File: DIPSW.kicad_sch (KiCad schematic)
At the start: 4 parts, among them SW1 OSCSEL

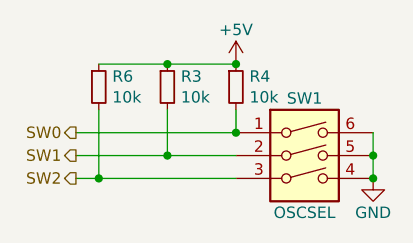
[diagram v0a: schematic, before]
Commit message: Migrate to KiCAD 6
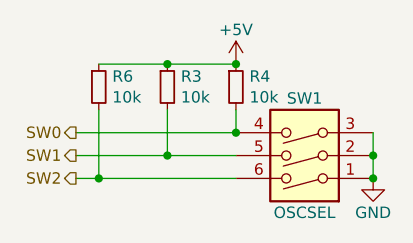
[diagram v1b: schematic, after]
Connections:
- net GND: now also SW1.1, SW1.2, SW1.3; no longer SW1.4, SW1.5, SW1.6
- net SW0: now also SW1.4; no longer SW1.1
- net SW1: now also SW1.5; no longer SW1.2
- net SW2: now also SW1.6; no longer SW1.3
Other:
- moved on the sheet: SW1
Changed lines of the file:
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@@
     (effects (font (size 1.27 1.27)) (justify right))
   )
-  (symbol (lib_id "Switch:SW_DIP_x03") (at 110.49 91.44 0)
+  (symbol (lib_id "Switch:SW_DIP_x03") (at 110.49 86.36 180) (unit 1)
     (in_bom yes) (on_board yes)
     (property "Reference" "SW1" (id 0) (at 110.49 82.55 0))
     (property "Value" "OSCSEL" (id 1) (at 110.49 95.25 0))
-    (property "Footprint" "stdpads:SW_DIP_SPSTx03_Slide_DSHP03TS_P1.27mm" (id 2) (at 110.49 91.44 0)
+    (property "Footprint" "stdpads:SW_DIP_SPSTx03_Slide_DSHP03TS_P1.27mm" (id 2) (at 110.49 86.36 0)
       (effects (font (size 1.27 1.27)) hide)
     )
-    (property "Datasheet" "~" (id 3) (at 110.49 91.44 0)
+    (property "Datasheet" "~" (id 3) (at 110.49 86.36 0)
       (effects (font (size 1.27 1.27)) hide)
     )
-    (property "LCSC Part" "C319051" (id 4) (at 110.49 91.44 0)
+    (property "LCSC Part" "C319051" (id 4) (at 110.49 86.36 0)
       (effects (font (size 1.27 1.27)) hide)
     )
@@
     (pin "6")
   )
-  (symbol (lib_id "Device:R_Small") (at 102.87 81.28 0)
+  (symbol (lib_id "Device:R_Small") (at 102.87 81.28 0) (unit 1)
     (in_bom yes) (on_board yes)
     (property "Reference" "R4" (id 0) (at 104.3686 80.1116 0)
@@
     (pin "2")
   )
-  (symbol (lib_id "Device:R_Small") (at 95.25 81.28 0)
+  (symbol (lib_id "Device:R_Small") (at 95.25 81.28 0) (unit 1)
     (in_bom yes) (on_board yes)
     (property "Reference" "R3" (id 0) (at 96.7486 80.1116 0)
@@
     (pin "2")
   )
-  (symbol (lib_id "power:GND") (at 118.11 91.44 0)
+  (symbol (lib_id "power:GND") (at 118.11 91.44 0) (unit 1)
     (in_bom yes) (on_board yes)
     (property "Reference" "#PWR0118" (id 0) (at 118.11 97.79 0)
@@
     (pin "1")
   )
-  (symbol (lib_id "Device:R_Small") (at 87.63 81.28 0)
+  (symbol (lib_id "Device:R_Small") (at 87.63 81.28 0) (unit 1)
     (in_bom yes) (on_board yes)
     (property "Reference" "R6" (id 0) (at 89.1286 80.1116 0)

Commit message: idk
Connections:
- net +5V renamed +3V3
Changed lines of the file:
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@@
     (pin "2")
   )
-  (symbol (lib_id "power:+5V") (at 102.87 78.74 0) (unit 1)
+  (symbol (lib_id "power:+3V3") (at 102.87 78.74 0) (unit 1)
     (in_bom yes) (on_board yes)
     (property "Reference" "#PWR0115" (id 0) (at 102.87 82.55 0)
       (effects (font (size 1.27 1.27)) hide)
     )
-    (property "Value" "+5V" (id 1) (at 102.87 74.93 0))
+    (property "Value" "+3V3" (id 1) (at 102.87 74.93 0))
     (property "Footprint" "" (id 2) (at 102.87 78.74 0)
       (effects (font (size 1.27 1.27)) hide)

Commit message: Prototype
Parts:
- SW1: value OSCSEL -> CFG
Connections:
- net SW0: now also R6.2, SW1.6; no longer R4.2, SW1.4
- net SW2: now also R4.2, SW1.4; no longer R6.2, SW1.6
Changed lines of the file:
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@@
     (effects (font (size 1.27 1.27)) (justify right))
   )
-  (hierarchical_label "SW0" (shape output) (at 85.09 86.36 180)
+  (hierarchical_label "SW0" (shape output) (at 85.09 91.44 180)
     (effects (font (size 1.27 1.27)) (justify right))
   )
-  (hierarchical_label "SW2" (shape output) (at 85.09 91.44 180)
+  (hierarchical_label "SW2" (shape output) (at 85.09 86.36 180)
     (effects (font (size 1.27 1.27)) (justify right))
   )
@@
     (in_bom yes) (on_board yes)
     (property "Reference" "SW1" (id 0) (at 110.49 82.55 0))
-    (property "Value" "OSCSEL" (id 1) (at 110.49 95.25 0))
+    (property "Value" "CFG" (id 1) (at 110.49 95.25 0))
     (property "Footprint" "stdpads:SW_DIP_SPSTx03_Slide_DSHP03TS_P1.27mm" (id 2) (at 110.49 86.36 0)
       (effects (font (size 1.27 1.27)) hide)
